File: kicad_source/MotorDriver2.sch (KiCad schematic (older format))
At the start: 25 parts, among them CN20 691322310004, CN21 BM05B-SRSS-TB, U1 TMC5130A-TA

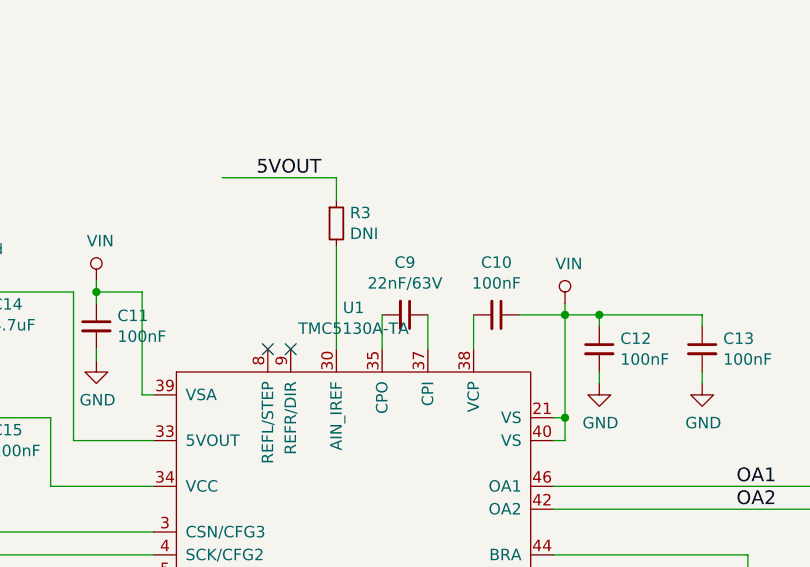
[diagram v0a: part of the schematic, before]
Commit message: updated part numbers
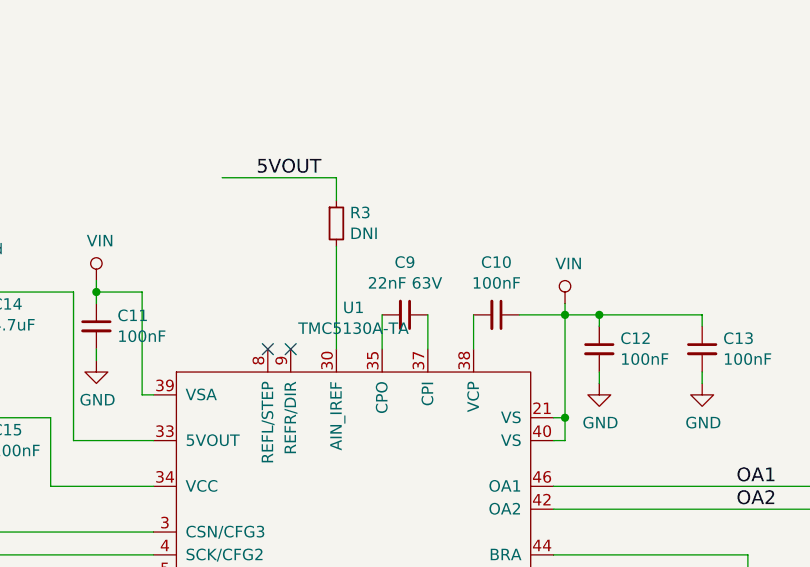
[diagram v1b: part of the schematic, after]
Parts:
- C9: value 22nF/63V -> 22nF 63V
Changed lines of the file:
@@
 P 6150 1900
 F 0 "C9" V 5921 1900 50  0000 C CNN
-F 1 "22nF/63V" V 6012 1900 50  0000 C CNN
+F 1 "22nF 63V" V 6012 1900 50  0000 C CNN
 F 2 "capacitors:C_0603" H 6150 1750 50  0001 C CNN
 F 3 "" H 6150 1900 50  0000 C CNN

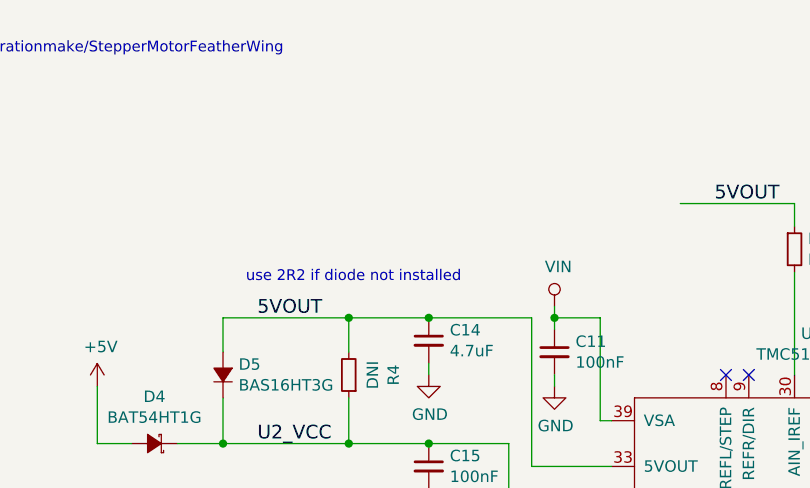
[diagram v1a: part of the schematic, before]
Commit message: corrected position of mounting holes for heat spreader, added information on input voltage
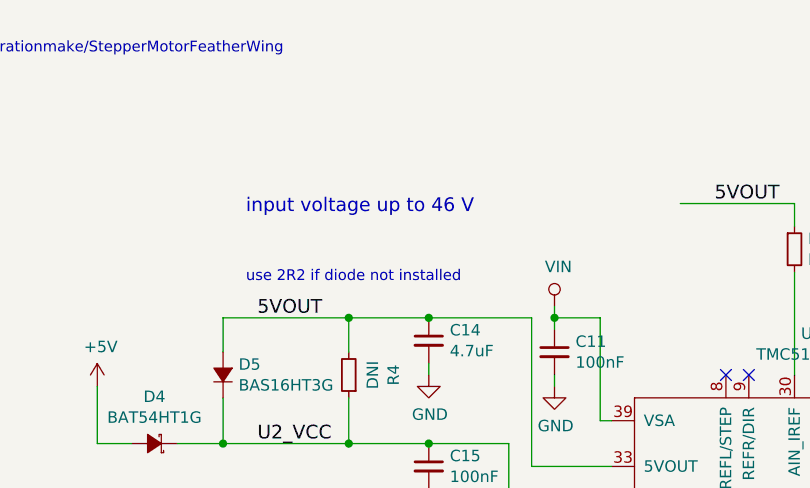
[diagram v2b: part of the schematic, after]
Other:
- note added: "input voltage up to 46 V"
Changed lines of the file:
@@
 Wire Wire Line
 	8400 3000 8400 3250
+Text Notes 3450 1350 0    60   ~ 0
+input voltage up to 46 V
 $EndSCHEMATC

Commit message: updated pdf files
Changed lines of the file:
@@
 encoding utf-8
 Sheet 5 6
-Title "HighPowerMotorFeatherWing"
-Date "2020-07-08"
+Title "StepperMotorFeatherWing"
+Date "2020-07-11"
 Rev "1.1"
 Comp "generationmake"
@@
 	1    0    0    1
 $EndComp
-Text Label 7600 2650 0    60   ~ 0
+Text Label 7700 2650 0    60   ~ 0
 OA1
-Text Label 7600 2750 0    60   ~ 0
+Text Label 7700 2750 0    60   ~ 0
 OA2
-Text Label 7750 3150 0    60   ~ 0
+Text Label 7700 3150 0    60   ~ 0
 OB1
-Text Label 7750 3250 0    60   ~ 0
+Text Label 7700 3250 0    60   ~ 0
 OB2
 $Comp

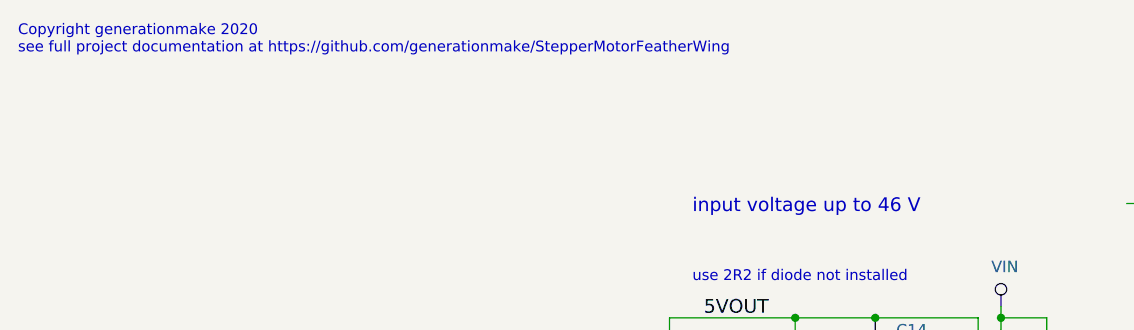
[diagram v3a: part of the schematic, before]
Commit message: corrected links and titles, generated schematic pdf and net list
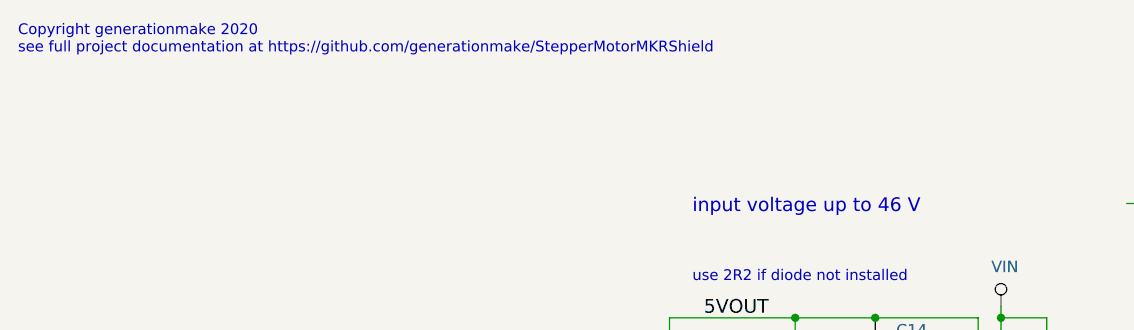
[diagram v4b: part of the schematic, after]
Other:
- note added: "Copyright generationmake 2020\nsee full project documentation at https://github.com/generationmake/StepperMotorMKRShield"
- note removed: "Copyright generationmake 2020\nsee full project documentation at https://github.com/generationmake/StepperMotorFeatherWing"
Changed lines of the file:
@@
 encoding utf-8
 Sheet 5 6
-Title "StepperMotorFeatherWing"
-Date "2020-07-11"
+Title "StepperMotorMKRShield"
+Date "2020-07-12"
 Rev "1.1"
 Comp "generationmake"
@@
 $EndDescr
 Text Notes 500  650  0    47   ~ 0
-Copyright generationmake 2020\nsee full project documentation at https://github.com/generationmake/StepperMotorFeatherWing
+Copyright generationmake 2020\nsee full project documentation at https://github.com/generationmake/StepperMotorMKRShield
 Text Notes 7000 6900 0    43   ~ 0
 You may redistribute and modify this documentation under the terms of the CERN OHL v.1.2. (http://ohwr.org/cernohl). \nThis documentation is distributed WITHOUT ANY EXPRESS OR IMPLIED WARRANTY, INCLUDING OF MERCHANTABILITY, SATISFACTORY \nQUALITY AND FITNESS FOR A PARTICULAR PURPOSE. Please see the CERN OHL v.1.2  for applicable conditions
